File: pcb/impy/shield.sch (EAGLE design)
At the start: 118 parts, among them J1 USB-2410-06, J2 SI-60062-F, J3 5V, U1 AD5933YRS, U10 LTC3406AB, U11 23LCV1024-I/SN, U13 ADG725BSU, U14 ADG725BSU, U15 ADG819BRT, U2 ADG704BRM, U3 AD8656ARZ, U4 M24C08WMN, U5 ADG706BRU, U6 DP83848I, U7 MIC2009A-1YM6, U8 AT25DF081A-SS, U9 SST25VF080B-80-4I-S2

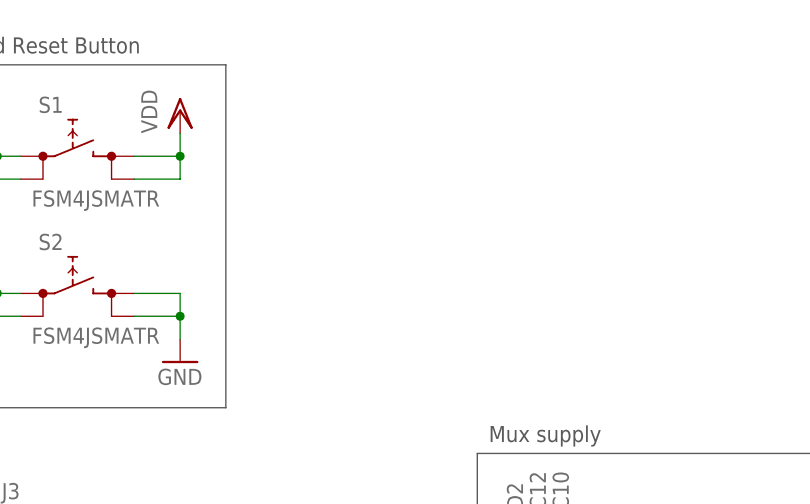
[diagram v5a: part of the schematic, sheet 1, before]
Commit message: * pcb/impy: (shield.sch, shield.brd) Add pull up resistors to I2C clock and data lines, the ones on the discovery board are too weak for a nice 400kHz signal.
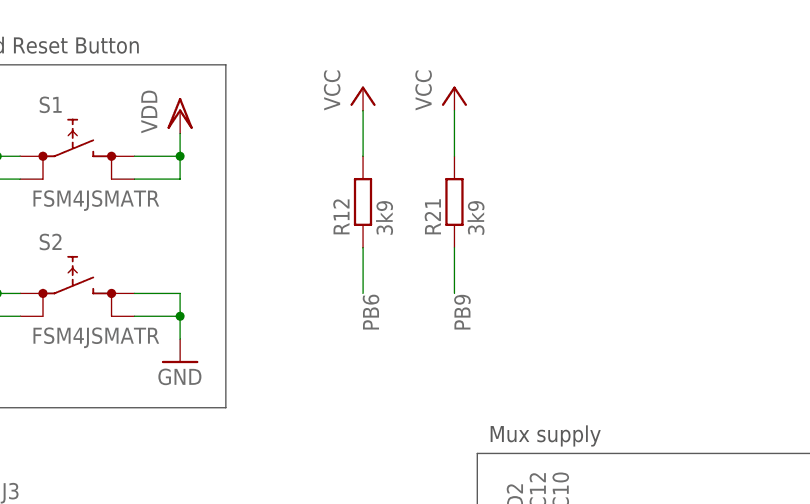
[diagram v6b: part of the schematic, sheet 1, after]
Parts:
- added R12, R21: 3k9, rcl:R-EU_R0603
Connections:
- net PB6: now also R12.1
- net PB9: now also R21.1
- net VCC: now also R12.2, R21.2
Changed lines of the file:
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@@
 <part name="AGND17" library="supply1" deviceset="AGND" device=""/>
 <part name="R20" library="rcl" deviceset="R-EU_" device="R0603" value="10"/>
+<part name="R12" library="rcl" deviceset="R-EU_" device="R0603" value="3k9"/>
+<part name="R21" library="rcl" deviceset="R-EU_" device="R0603" value="3k9"/>
+<part name="P+38" library="supply1" deviceset="VCC" device=""/>
+<part name="P+39" library="supply1" deviceset="VCC" device=""/>
 </parts>
 <sheets>
@@
 <instance part="AGND8" gate="VR1" x="256.54" y="-5.08" rot="MR0"/>
 <instance part="AGND9" gate="VR1" x="256.54" y="17.78" rot="MR0"/>
+<instance part="R12" gate="G$1" x="200.66" y="73.66" rot="R90"/>
+<instance part="R21" gate="G$1" x="210.82" y="73.66" rot="R90"/>
+<instance part="P+38" gate="VCC" x="200.66" y="86.36"/>
+<instance part="P+39" gate="VCC" x="210.82" y="86.36"/>
 </instances>
 <busses>
@@
 <label x="86.36" y="58.42" size="1.778" layer="95"/>
 </segment>
+<segment>
+<pinref part="R21" gate="G$1" pin="1"/>
+<wire x1="210.82" y1="68.58" x2="210.82" y2="63.5" width="0.1524" layer="91"/>
+<label x="210.82" y="63.5" size="1.778" layer="95" rot="R270"/>
+</segment>
 </net>
 <net name="PB6" class="0">
@@
 <wire x1="71.12" y1="53.34" x2="63.5" y2="53.34" width="0.1524" layer="91"/>
 <label x="63.5" y="53.34" size="1.778" layer="95" rot="R180"/>
+</segment>
+<segment>
+<pinref part="R12" gate="G$1" pin="1"/>
+<wire x1="200.66" y1="68.58" x2="200.66" y2="63.5" width="0.1524" layer="91"/>
+<label x="200.66" y="63.5" size="1.778" layer="95" rot="R270"/>
 </segment>
 </net>
@@
 <junction x="256.54" y="10.16"/>
 </segment>
-</net>
+<segment>
+<pinref part="R12" gate="G$1" pin="2"/>
+<pinref part="P+38" gate="VCC" pin="VCC"/>
+<wire x1="200.66" y1="78.74" x2="200.66" y2="83.82" width="0.1524" layer="91"/>
+</segment>
+<segment>
+<pinref part="R21" gate="G$1" pin="2"/>
+<pinref part="P+39" gate="VCC" pin="VCC"/>
+<wire x1="210.82" y1="78.74" x2="210.82" y2="83.82" width="0.1524" layer="91"/>
+</segment>
+</net>

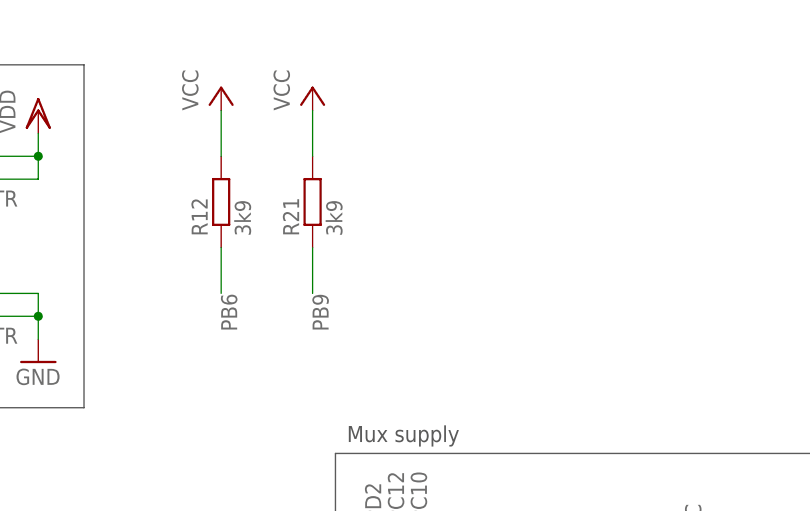
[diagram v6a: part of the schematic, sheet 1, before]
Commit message: * pcb/impy: (shield.sch, shield.brd) Add pull down resistor to PA9 (USB device VBUS pin) to prevent the green LED from turning on while the internal pull down is not configured.
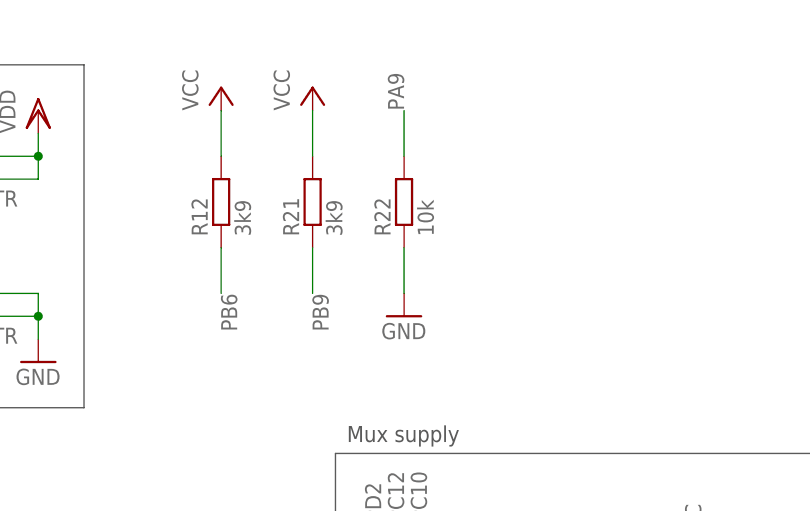
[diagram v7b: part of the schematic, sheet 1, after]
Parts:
- added R22: 10k, rcl:R-EU_R0603
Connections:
- net GND: now also R22.1
- net PA9: now also R22.2
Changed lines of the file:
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@@
 <part name="P+38" library="supply1" deviceset="VCC" device=""/>
 <part name="P+39" library="supply1" deviceset="VCC" device=""/>
+<part name="GND6" library="supply1" deviceset="GND" device=""/>
+<part name="R22" library="rcl" deviceset="R-EU_" device="R0603" value="10k"/>
 </parts>
 <sheets>
@@
 <instance part="P+38" gate="VCC" x="200.66" y="86.36"/>
 <instance part="P+39" gate="VCC" x="210.82" y="86.36"/>
+<instance part="GND6" gate="1" x="220.98" y="60.96"/>
+<instance part="R22" gate="G$1" x="220.98" y="73.66" rot="R90"/>
 </instances>
 <busses>
@@
 <pinref part="JP2" gate="A" pin="49"/>
 <wire x1="60.96" y1="20.32" x2="71.12" y2="20.32" width="0.1524" layer="91"/>
+</segment>
+<segment>
+<pinref part="GND6" gate="1" pin="GND"/>
+<pinref part="R22" gate="G$1" pin="1"/>
+<wire x1="220.98" y1="63.5" x2="220.98" y2="68.58" width="0.1524" layer="91"/>
 </segment>
 </net>
@@
 <wire x1="96.52" y1="27.94" x2="96.52" y2="38.1" width="0.1524" layer="91"/>
 </segment>
-</net>
+<segment>
+<pinref part="R22" gate="G$1" pin="2"/>
+<wire x1="220.98" y1="78.74" x2="220.98" y2="83.82" width="0.1524" layer="91"/>
+<label x="220.98" y="83.82" size="1.778" layer="95" rot="R90"/>
+</segment>
+</net>

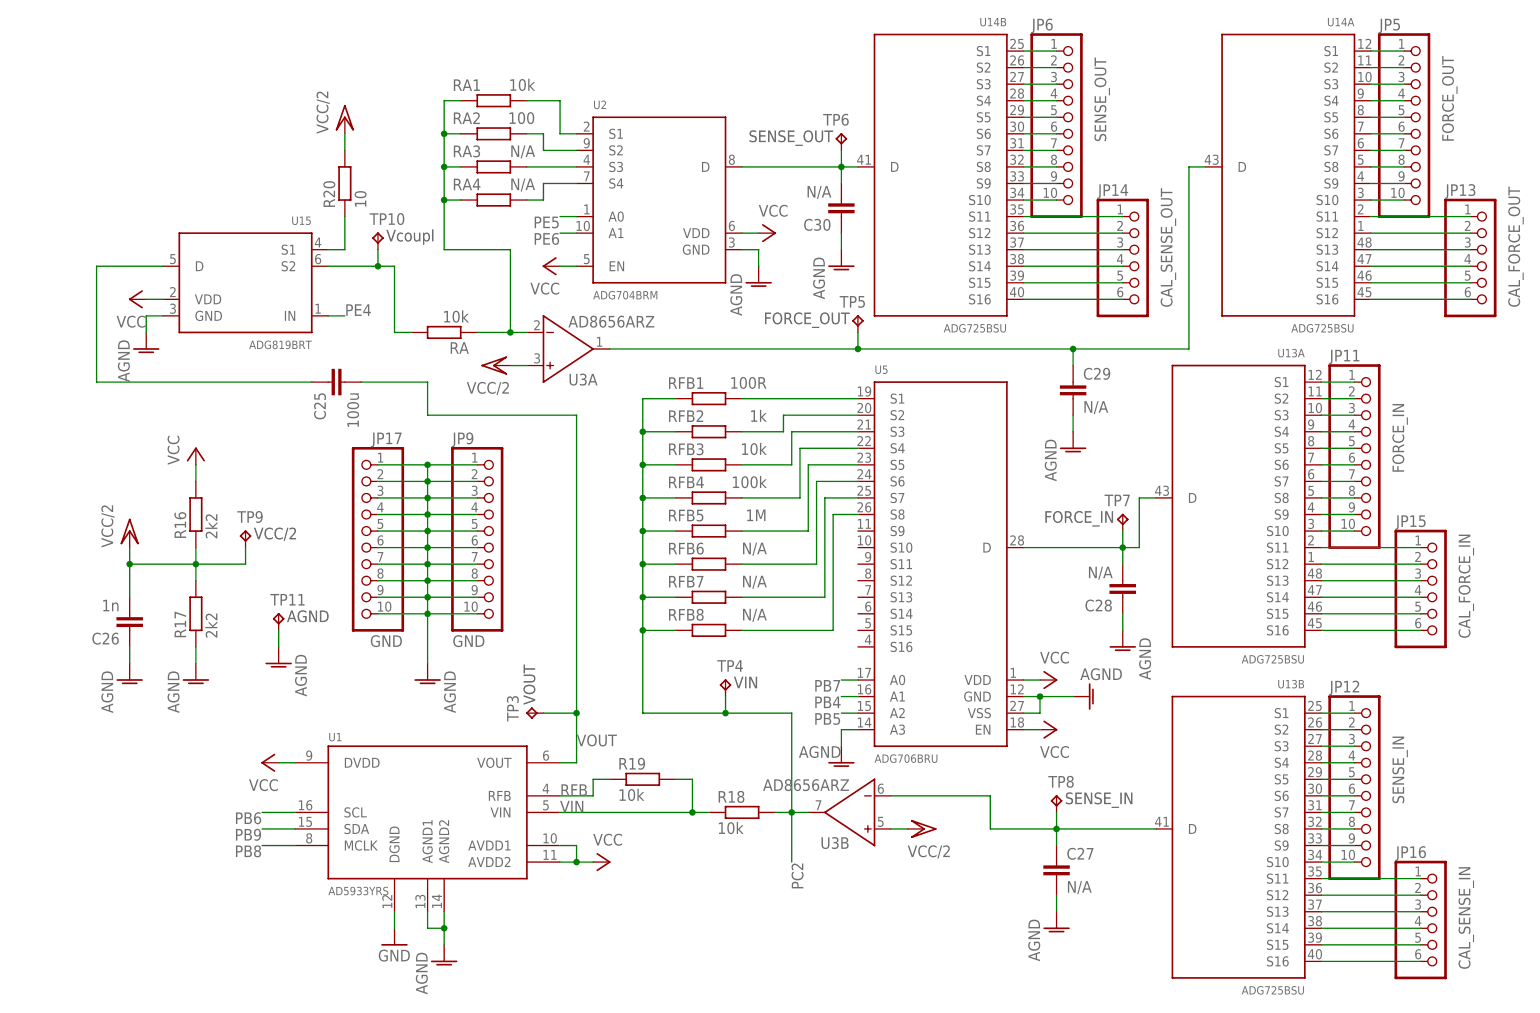
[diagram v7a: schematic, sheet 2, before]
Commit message: * pcb/impy: (shield.sch) Add various compensation capacitors to the op amps.
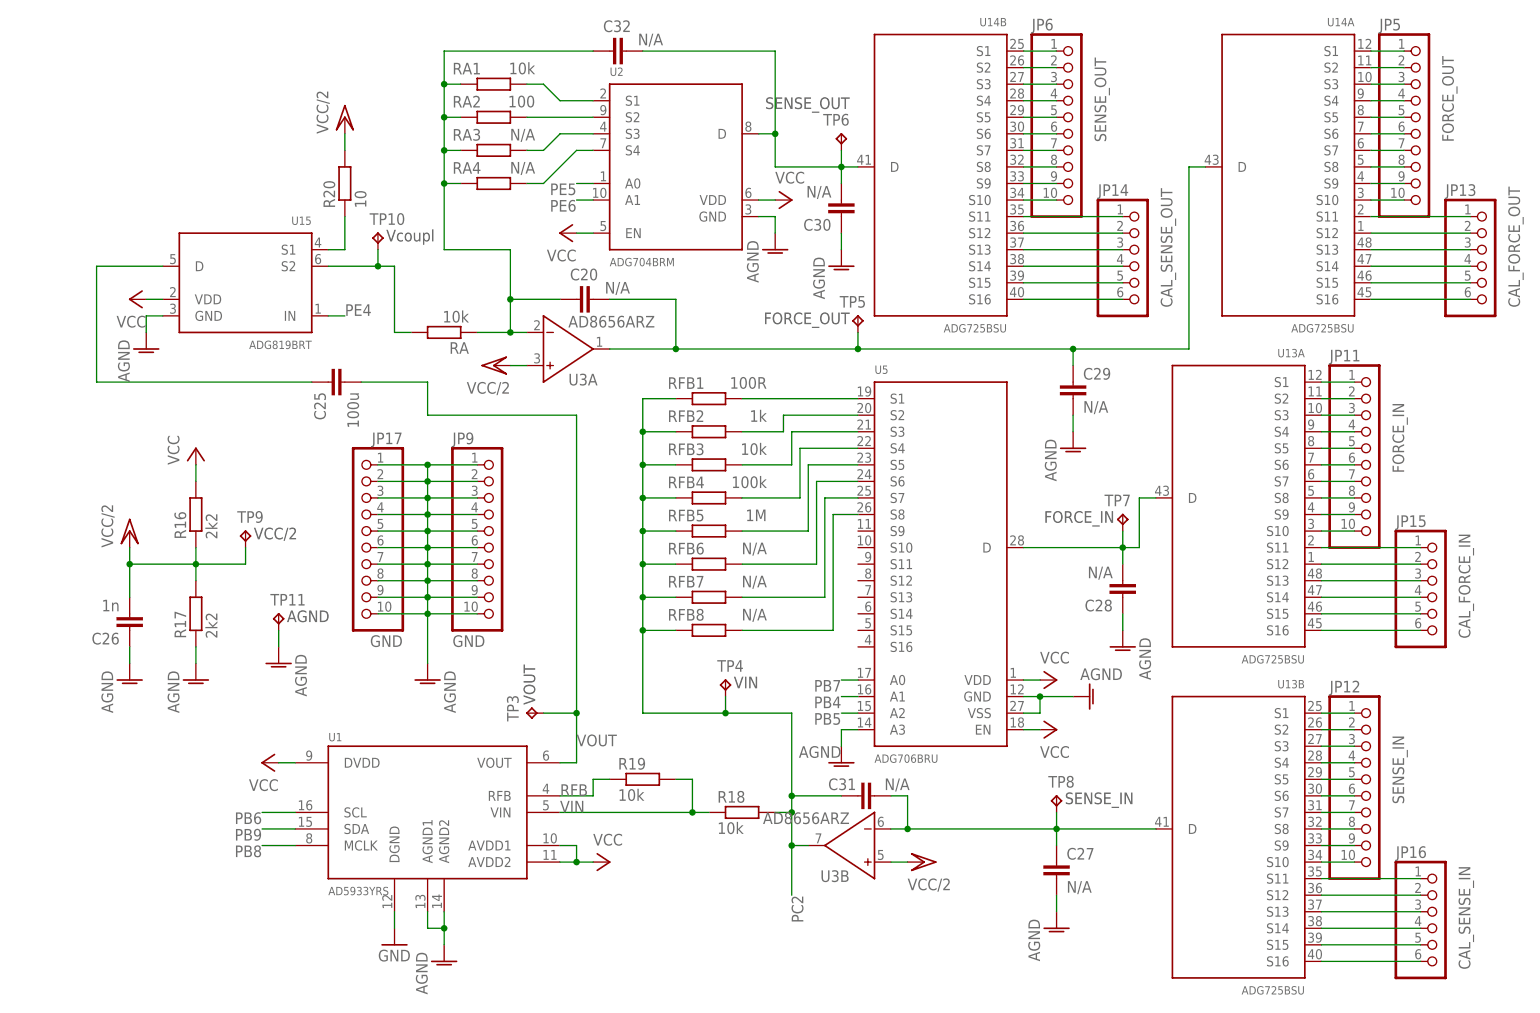
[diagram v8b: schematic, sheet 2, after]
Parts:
- added C20, C31, C32: N/A, rcl:C-EUC0603
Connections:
- net N$12: now also C31.2
- net N$14: now also C20.2
- net N$15: now also C32.2
- net N$3: now also C20.1, C32.1
- net PC2: now also C31.1
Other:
- moved on the sheet: RA1, RA2, RA3, RA4, U2, U3B
